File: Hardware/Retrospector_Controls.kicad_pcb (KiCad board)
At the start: 2 copper layers, 60 x 110 mm, 32 parts, among them J1 Conn_01x08_Female, J10 Feedback_CV, J11 Audio_In_R, J12 Audio_Out_R, J13 Audio_Out_L, J14 Filter, J2 Conn_01x08_Female, J3 Conn_01x08_Female, J4 Conn_01x08_Female, J5 Audio_In_L, J6 Delay_CV_L, J7 Mix_CV, J8 Delay_CV_R, J9 Clock, U1 TB62781FNG

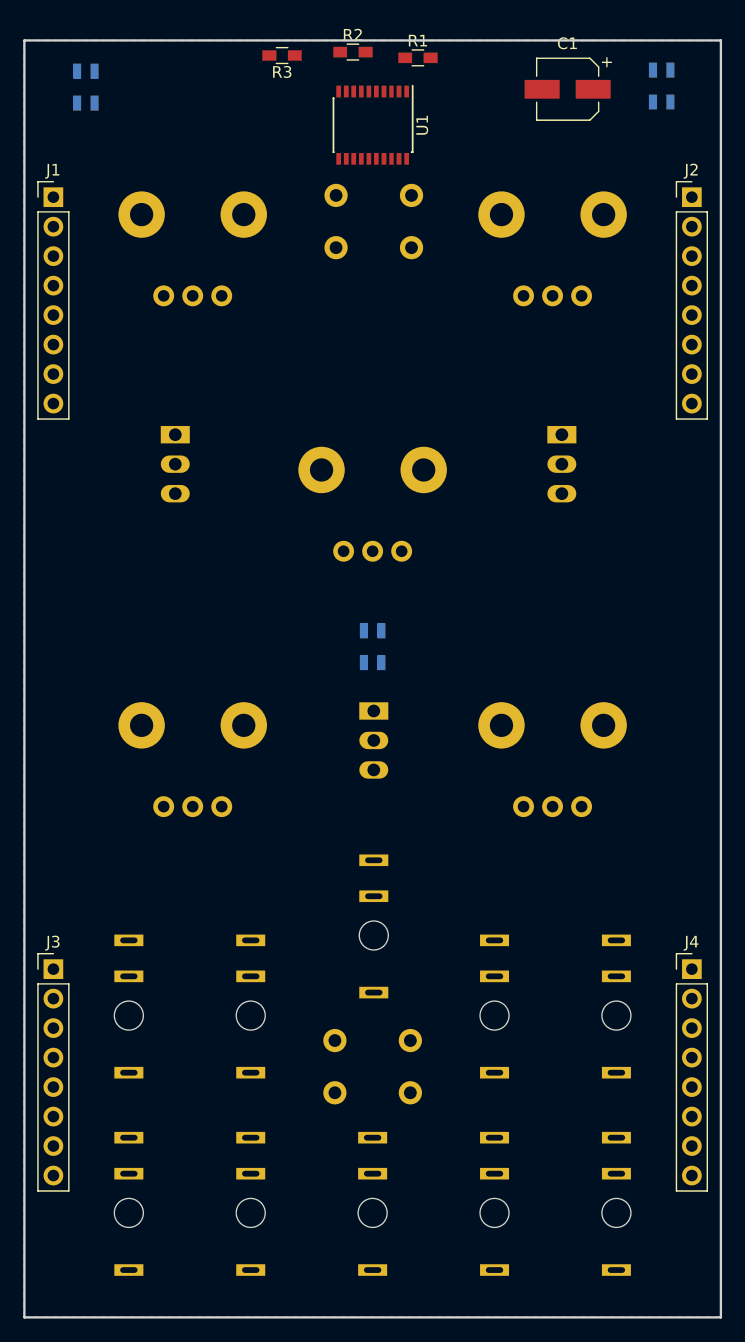
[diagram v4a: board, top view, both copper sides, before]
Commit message: Routed controls PCB
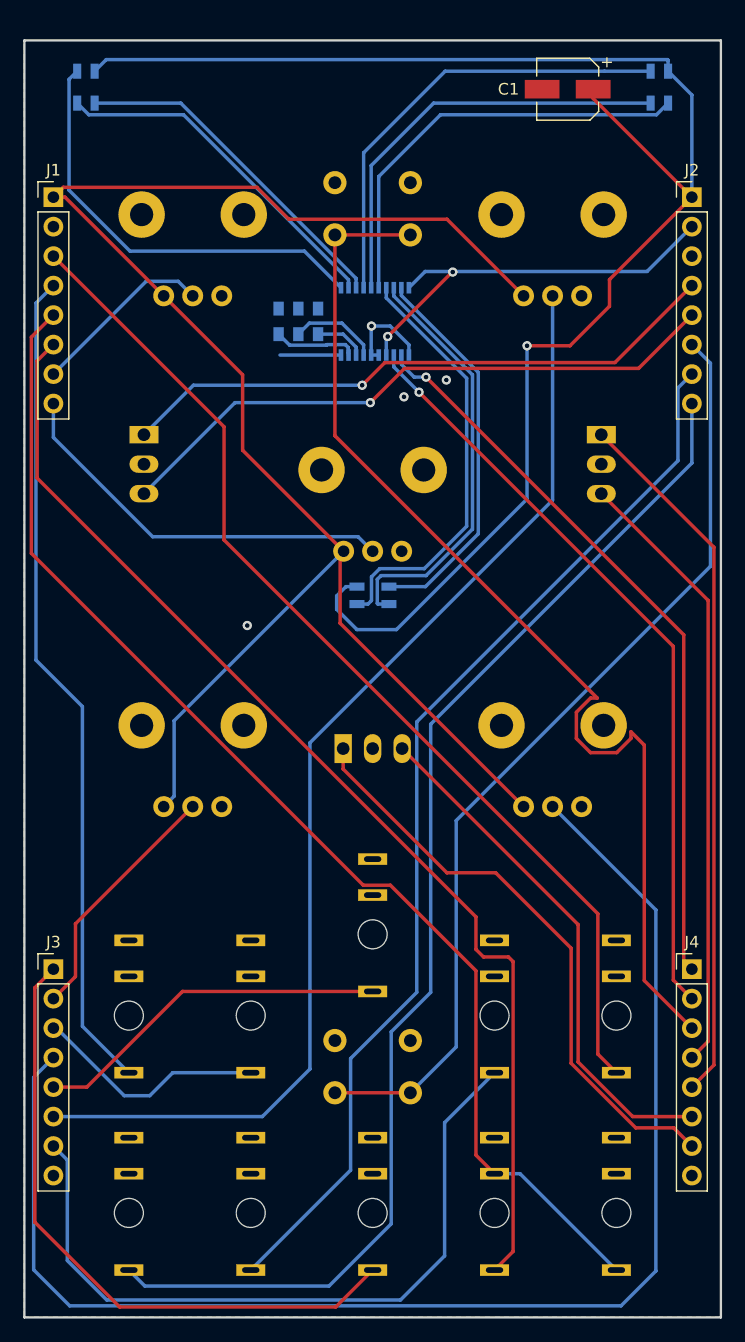
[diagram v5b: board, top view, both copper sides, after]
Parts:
- R1, R2, R3, U1: moved to B.Cu
- moved D1 49.6 mm to (105.3, 54.0)
- moved D2 49.4 mm to (154.7, 54.0)
- moved R1 24.9 mm to (123.6, 74.2), turned to 90 degrees
- moved R2 23.4 mm to (125.3, 74.2), turned to 90 degrees
- moved R3 22.9 mm to (121.9, 74.2), turned to 90 degrees
- moved U1 16.9 mm to (130.2, 74.2), turned to 90 degrees
- moved D3 4.40 mm to (130.0, 97.8), turned to 90 degrees
- moved WIDTH_MODE1 3.40 mm to (149.7, 86.5)
- moved DELAY_MODE1 2.70 mm to (110.3, 86.5)
- moved LOCK1 1.10 mm to (130.0, 64.5)
- moved FILTER_MODE1 0.71 mm to (130.0, 111.0), turned to 0 degrees
- moved J14 0.14 mm to (130.0, 127.0)
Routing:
- net +3.3VA: track 0.00 -> 143.3 mm
- net +5V: track 0.00 -> 134.4 mm, vias 0 -> 1
- net /FEEDBACK_POT: track 0.00 -> 118.8 mm
- net /EXT_AUDIO_OUT_R: track 0.00 -> 106.8 mm
- net /EXT_AUDIO_IN_L: track 0.00 -> 106.6 mm
- net /EXT_AUDIO_IN_R: track 0.00 -> 99.2 mm
- net /DELAY_POT_L: track 0.00 -> 99.1 mm
- net /LINK_BTN: track 0.00 -> 94.4 mm
- net /EXT_AUDIO_OUT_L: track 0.00 -> 92.9 mm
- net /DELAY_CV_L: track 0.00 -> 90.4 mm
- net /RESET: track 0.00 -> 82.3 mm
- net /DELAY_CV_R: track 0.00 -> 71.7 mm
- net /LED_SPI_CLK: track 0.00 -> 66.1 mm, vias 0 -> 1
- net /LED_SPI_DATA: track 0.00 -> 63.9 mm, vias 0 -> 1
- net /FEEDBACK_CV: track 0.00 -> 63.4 mm
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
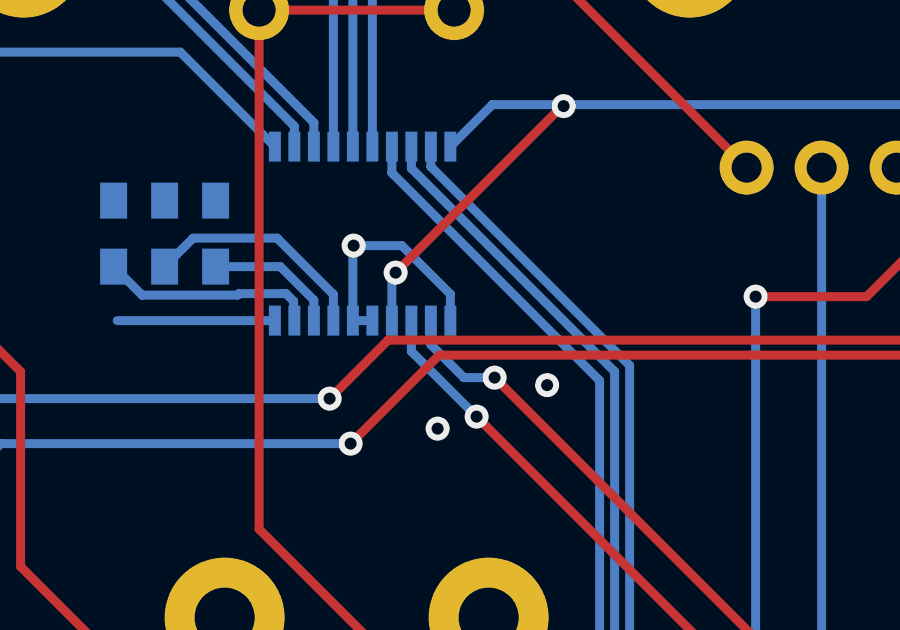
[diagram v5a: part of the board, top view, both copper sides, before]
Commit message: Final updates to v2 PCBs for production; USB DFU Mode working
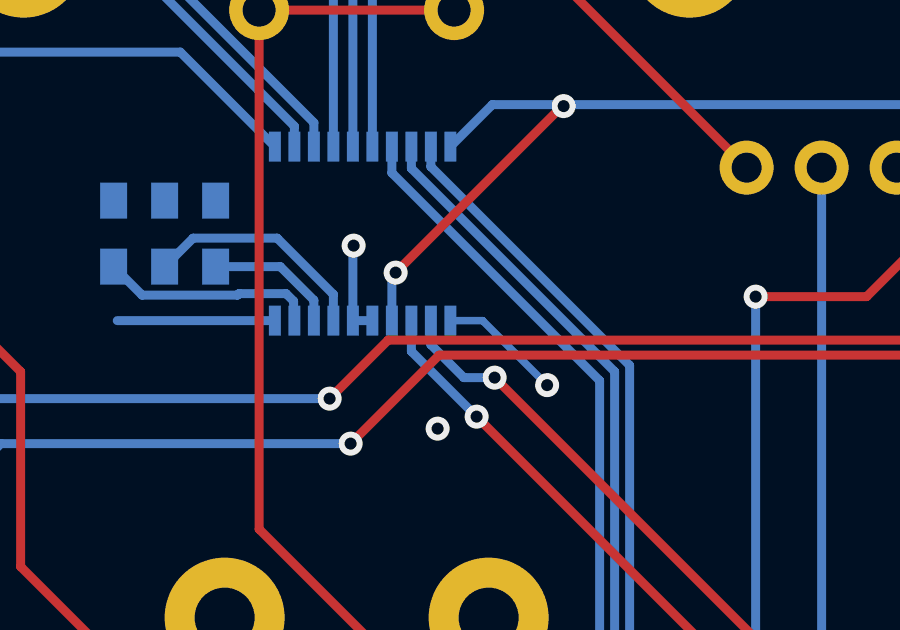
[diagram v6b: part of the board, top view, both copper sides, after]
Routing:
- net GND: track 13.2 -> 12.5 mm
